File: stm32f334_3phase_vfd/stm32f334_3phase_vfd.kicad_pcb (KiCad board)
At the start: 4 copper layers, 80 x 80 mm, 55 parts, among them J1 HV, J10 MH, J101 Conn_01x04, J102 Conn_01x04, J103 Conn_01x04, J104 Conn_01x04, J105 Conn_01x02, J106 Conn_01x04, J11 MH, J2 PHA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

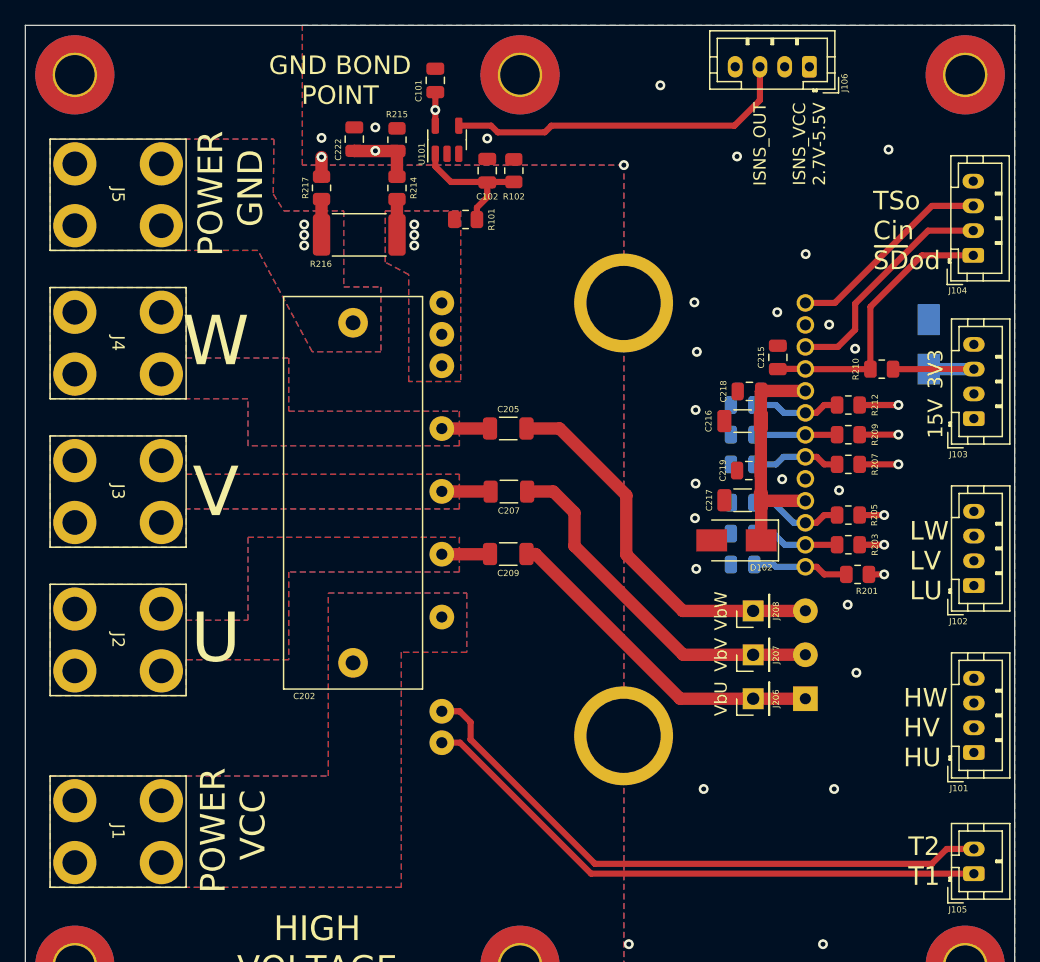
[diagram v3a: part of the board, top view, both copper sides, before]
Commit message: update schematic
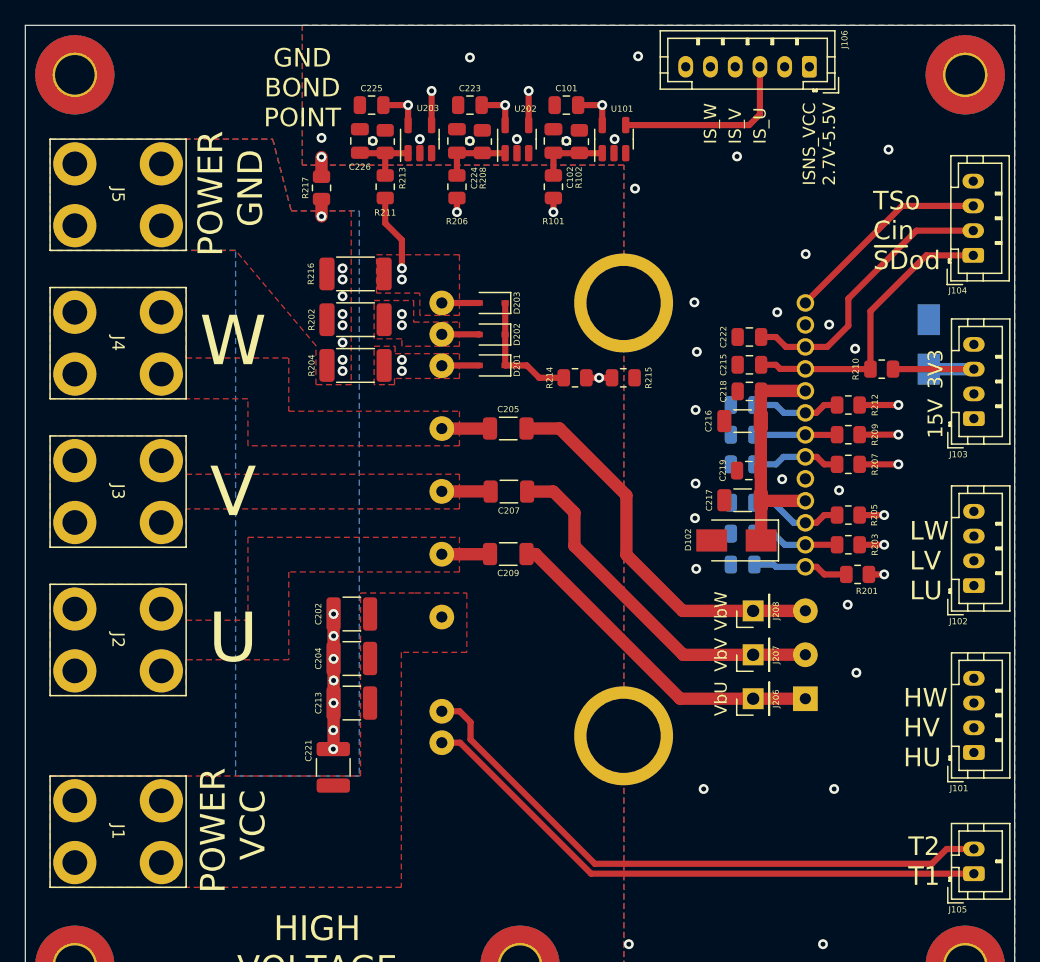
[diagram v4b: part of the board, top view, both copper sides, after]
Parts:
- removed J11: MH, MountingHole:MountingHole_3.2mm_M3_Pad_TopBottom
- added C204: C1210C104KCRACTU, Capacitor_SMD:C_1210_3225Metric, F.Cu at (109.9, 88.4)
- added C213: C1210C104KCRACTU, Capacitor_SMD:C_1210_3225Metric, F.Cu at (109.9, 92.0)
- added C221: C1210C104KCRACTU, Capacitor_SMD:C_1210_3225Metric, F.Cu at (108.4, 97.2)
- added C223: 100n, Capacitor_SMD:C_0805_2012Metric, F.Cu at (119.5, 43.6)
- added C224: 10p, Capacitor_SMD:C_0805_2012Metric, F.Cu at (118.4, 46.5)
- added C225: 100n, Capacitor_SMD:C_0805_2012Metric, F.Cu at (111.5, 43.6)
- added C226: 10p, Capacitor_SMD:C_0805_2012Metric, F.Cu at (110.5, 46.5)
- added D201: BAT48JFILM, Diode_SMD:D_SOD-323, F.Cu at (121.2, 64.7)
- added D202: BAT48JFILM, Diode_SMD:D_SOD-323, F.Cu at (121.2, 62.2)
- added D203: BAT48JFILM, Diode_SMD:D_SOD-323, F.Cu at (121.2, 59.6)
- added R202: WSL2010R0330FEA, Resistor_SMD:R_2010_5025Metric, F.Cu at (110.2, 61.0)
- added R204: WSL2010R0330FEA, Resistor_SMD:R_2010_5025Metric, F.Cu at (110.2, 64.7)
- added R206: 1k, Resistor_SMD:R_0805_2012Metric, F.Cu at (118.4, 50.2)
- added R208: 1k, Resistor_SMD:R_0805_2012Metric, F.Cu at (120.5, 46.6)
- added R211: 1k, Resistor_SMD:R_0805_2012Metric, F.Cu at (112.6, 50.2)
- added R213: 1k, Resistor_SMD:R_0805_2012Metric, F.Cu at (112.6, 46.6)
- added U202: INA180B1, Package_TO_SOT_SMD:SOT-23-5, F.Cu at (123.2, 46.4)
- added U203: INA180B1, Package_TO_SOT_SMD:SOT-23-5, F.Cu at (115.4, 46.4)
- C202: value B32774X8305K000 -> C1210C104KCRACTU; footprint Capacitor_THT:C_Rect_L31.5mm_W11.0mm_P27.50mm_MKS4 -> Capacitor_SMD:C_1210_3225Metric
- J106: value Conn_01x04 -> Conn_01x06; footprint Connector_JST:JST_PH_B4B-PH-K_1x04_P2.00mm_Vertical -> Connector_JST:JST_PH_B6B-PH-K_1x06_P2.00mm_Vertical
- R216: value LVM25FVR020E-TR -> WSL2010R0330FEA; footprint Resistor_SMD:R_2512_6332Metric_Pad1.40x3.35mm_HandSolder -> Resistor_SMD:R_2010_5025Metric
- moved C222 35.7 mm to (142.1, 62.4), turned to 180 degrees
- moved R215 26.6 mm to (131.8, 65.7), turned to 0 degrees
- moved C202 23.6 mm to (109.9, 84.8), turned to 180 degrees
- moved R214 21.0 mm to (128.0, 65.7), turned to 180 degrees
- moved U101 13.5 mm to (131.1, 46.4)
- moved C101 10.8 mm to (127.2, 43.6), turned to 180 degrees
- moved R101 7.58 mm to (126.2, 50.2), turned to 90 degrees
- moved C102 5.86 mm to (126.2, 46.5)
- moved R102 5.80 mm to (128.3, 46.6)
- moved R216 3.17 mm to (110.2, 57.3)
- moved C215 2.38 mm to (142.1, 64.7), turned to 180 degrees
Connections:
- net /power/ISENSE_OUT renamed /power/IS_U
- C202 pad 1: GNDPWR -> /power/HV
- C202 pad 2: /power/HV -> GNDPWR
- J106 pad 4: GND -> /power/IS_V
- R101 pad 1: /power/N -> /power/NU
- R214 pad 2: /power/N -> Net-(D201-Pad1)
- R216 pad 1: /power/N -> /power/NW
- U201 pad 18: /power/N -> /power/NW
- U201 pad 19: /power/N -> /power/NV
- U201 pad 20: /power/N -> /power/NU
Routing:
- net /power/IS_W: track 0.00 -> 28.3 mm, vias 0 -> 1
- net /power/Cin: track 68.1 -> 42.5 mm
- net /power/NU: track 0.00 -> 23.4 mm, vias 0 -> 3
- net /power/IS_V: track 0.00 -> 22.5 mm, vias 0 -> 1
- net /power/NV: track 0.00 -> 17.5 mm, vias 0 -> 3
- net /power/IS_U: track 28.3 -> 15.1 mm
- net Net-(D201-Pad1): track 0.00 -> 10.2 mm
- net /power/ISENSE_VCC: track 35.8 -> 45.8 mm, vias 1 -> 3
- net GNDPWR: track 2.89 -> 12.4 mm, vias 3 -> 16
- net /power/NW: track 0.00 -> 9.27 mm, vias 0 -> 2
- net Net-(C224-Pad1): track 0.00 -> 5.75 mm
- net Net-(C226-Pad1): track 0.00 -> 5.74 mm
- net Net-(C102-Pad1): track 11.2 -> 5.80 mm
- net /power/N: track 2.88 -> 0.00 mm, vias 3 -> 0
- net /power/~{sd}_od: track 22.6 -> 23.9 mm
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- added copper zone on F.Cu, net /power/NU
- added copper zone on In1.Cu, net /power/NU
- added copper zone on In2.Cu, net /power/NU
- added copper zone on F.Cu, net /power/NV
- added copper zone on In1.Cu, net /power/NV
- added copper zone on In2.Cu, net /power/NV
- added copper zone on F.Cu, net /power/NW
- added copper zone on In1.Cu, net /power/NW
- added copper zone on In2.Cu, net /power/NW
- removed copper zone on B.Cu, net /power/HV
- removed copper zone on B.Cu, net /power/N
- removed copper zone on F.Cu, net /power/N
- removed copper zone on In1.Cu, net /power/N
- removed copper zone on In2.Cu, net /power/N
- removed copper zone on B.Cu, net /power/U
- removed copper zone on B.Cu, net /power/V
- removed copper zone on B.Cu, net /power/W
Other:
- board text added: "IS_U"
- board text added: "IS_V"
- board text added: "IS_W"
- board text removed: "ISNS_OUT"

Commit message: small updates in the schematic
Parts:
- moved R201 0.30 mm to (150.8, 81.3)
- moved R205 0.30 mm to (150.1, 77.1)
- moved R207 0.30 mm to (150.1, 72.4)
- moved R212 0.30 mm to (150.1, 68.2)
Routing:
- net /power/T2: track 49.5 -> 51.9 mm
- net /power/T1: track 47.4 -> 49.3 mm
